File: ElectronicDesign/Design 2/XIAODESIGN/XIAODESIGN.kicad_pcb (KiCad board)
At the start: 2 copper layers, 92 x 50 mm, 24 parts, among them U1 XIAO-ESP32-C3-SMD, U2 MPR121QR2, U3 MPU-6050_C24112, U6 S2B-PH-K-S

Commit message: Continued Routing on the PCB Design , implementation of delay effect started and vector method for effects implemented
Vector method for effects will allow for the user to change the order of the effects using hopefully a draggable component from a previous project
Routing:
- net Net-(U2-ELE1): track 0.00 -> 50.1 mm, vias 0 -> 3
- net /INT_GYRO: track 7.58 -> 20.4 mm, vias 0 -> 2
- net Net-(U2-VREG): track 0.00 -> 8.58 mm

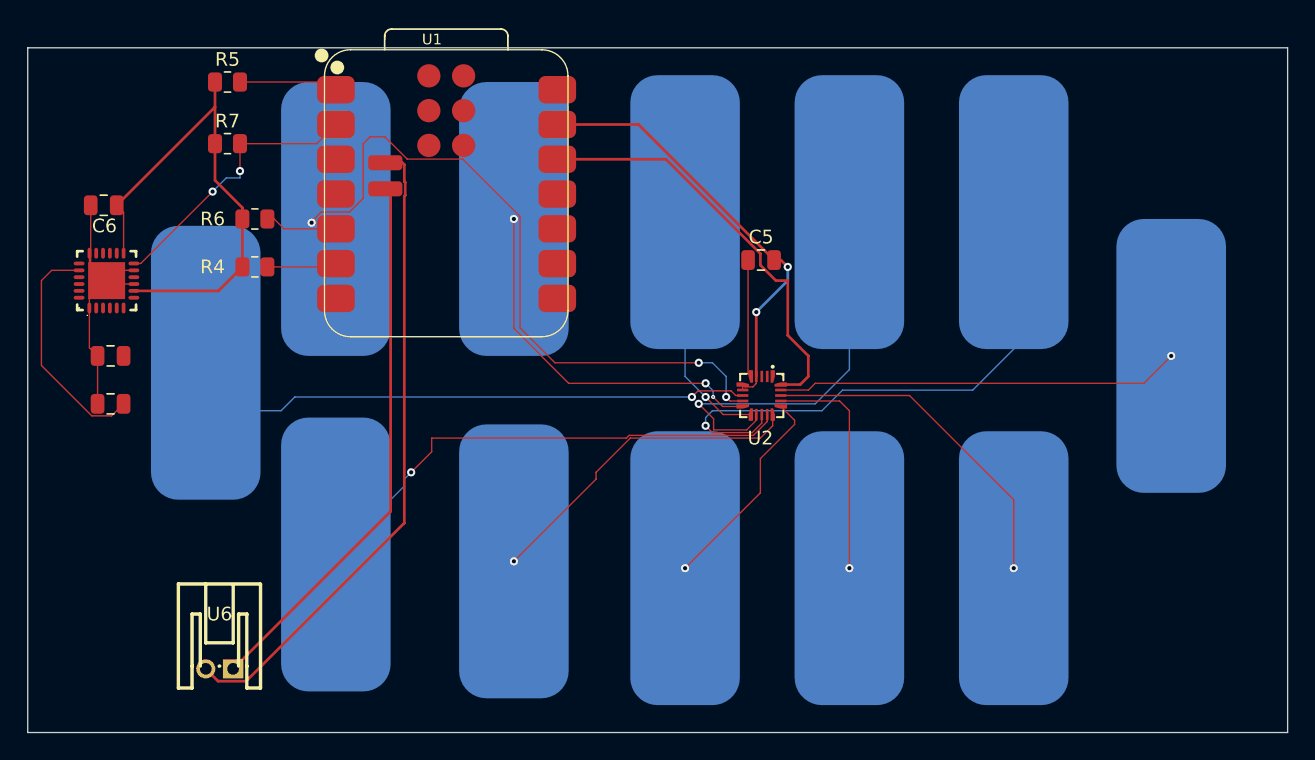
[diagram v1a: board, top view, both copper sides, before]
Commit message: Updates to draggable component , Re tracing the pcb routing to change the position of the microcontroller
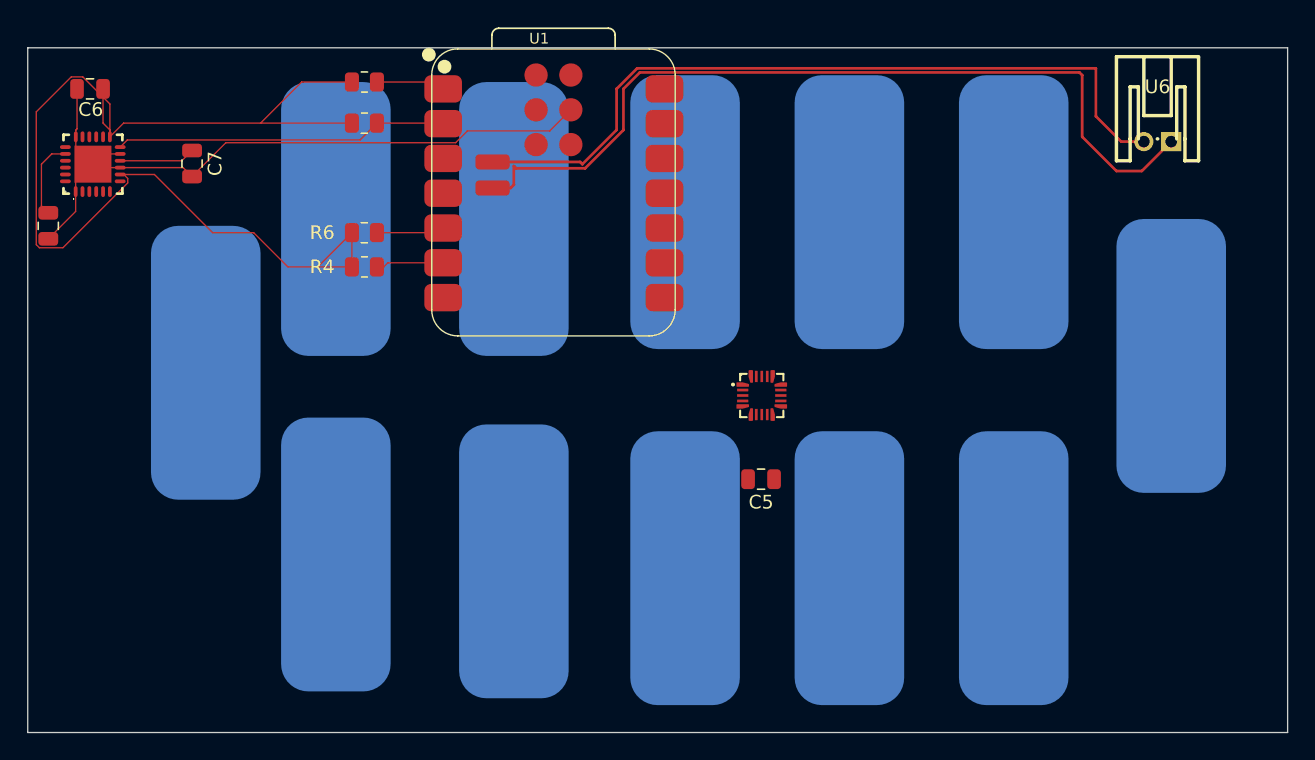
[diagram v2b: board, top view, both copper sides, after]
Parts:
- moved U6 78.6 mm to (128.5, 120.8)
- moved C5 16.0 mm to (99.5, 145.5), turned to 180 degrees
- moved C7 15.3 mm to (58.0, 122.5), turned to -90 degrees
- moved C8 13.8 mm to (47.5, 127.0), turned to 90 degrees
- moved R7 10.1 mm to (70.6, 119.5)
- moved R5 10.0 mm to (70.6, 116.5)
- moved C6 8.56 mm to (50.5, 117.0)
- moved U3 8.56 mm to (50.8, 122.5)
- moved R6 8.06 mm to (70.6, 127.5)
- moved R4 8.00 mm to (70.6, 130.0)
- moved U1 7.83 mm to (75.5, 135.1)
- turned U2 to -90 degrees
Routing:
- net Net-(U2-ELE1): track 50.1 -> 0.00 mm, vias 3 -> 0
- net Net-(U2-ELE0): track 41.4 -> 0.00 mm, vias 1 -> 0
- net Net-(U2-ELE5): track 40.4 -> 0.00 mm, vias 1 -> 0
- net Net-(U2-ELE6): track 36.9 -> 0.00 mm, vias 1 -> 0
- net Net-(U2-ELE4): track 29.7 -> 0.00 mm, vias 1 -> 0
- net Net-(U2-ELE11): track 29.5 -> 0.00 mm, vias 1 -> 0
- net Net-(U2-ELE2): track 27.3 -> 0.00 mm, vias 3 -> 0
- net Net-(U2-ELE10): track 25.2 -> 0.00 mm, vias 1 -> 0
- net Net-(U2-ELE7): track 24.1 -> 0.00 mm, vias 1 -> 0
- net +BATT: track 40.0 -> 62.3 mm
- net Net-(U2-ELE3): track 18.0 -> 0.00 mm, vias 1 -> 0
- net +3V3: track 67.7 -> 84.5 mm
- net Net-(U2-ELE9): track 16.8 -> 0.00 mm, vias 1 -> 0
- net Net-(U2-ELE8): track 15.5 -> 0.00 mm, vias 1 -> 0
- net Net-(U3-CPOUT): track 17.1 -> 5.82 mm
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
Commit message: Update to the routing
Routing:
- net GND: track 52.4 -> 157.2 mm, vias 0 -> 4
- net /SCL: track 4.96 -> 80.5 mm, vias 0 -> 2
- net Net-(U2-ELE2): track 0.00 -> 61.6 mm, vias 0 -> 1
- net /SDA: track 4.98 -> 63.9 mm, vias 0 -> 2
- net Net-(U2-ELE7): track 0.00 -> 53.9 mm, vias 0 -> 1
- net /IRQ_TS: track 5.04 -> 55.9 mm
- net Net-(U2-ELE1): track 0.00 -> 50.6 mm, vias 0 -> 1
- net Net-(U2-ELE0): track 0.00 -> 44.7 mm, vias 0 -> 1
- net Net-(U2-ELE6): track 0.00 -> 38.7 mm, vias 0 -> 1
- net Net-(U2-ELE4): track 0.00 -> 36.2 mm, vias 0 -> 1
- net Net-(U2-ELE11): track 0.00 -> 31.6 mm, vias 0 -> 1
- net Net-(U2-ELE3): track 0.00 -> 29.3 mm, vias 0 -> 1
- net Net-(U2-ELE10): track 0.00 -> 26.6 mm, vias 0 -> 1
- net +3V3: track 84.5 -> 60.4 mm, vias 0 -> 2
- net Net-(U2-ELE9): track 0.00 -> 23.6 mm, vias 0 -> 1
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
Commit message: Updated the draggable component constructor and implemented an array of the draggable components
Name of the effect connected to the draggable component is now passed through in the constructor , an array of the draggable components equal in size to the number of effects in the synth
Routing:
- net +3V3: track 60.4 -> 105.1 mm, vias 2 -> 6
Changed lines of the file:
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@@
+	)
+	(segment
+		(start 69.675 116.5)
+		(end 71.575 114.6)
+		(width 0.2)
+		(layer "F.Cu")
+		(net "+3V3")
 	)
 	(segment
@@
 	)
 	(segment
+		(start 61.5 124.5)
+		(end 62.5 123.5)
+		(width 0.2)
+		(layer "F.Cu")
+		(net "+3V3")
+	)
+	(segment
 		(start 53.01 123.25)
 		(end 54.26 124.5)
@@
 	)
 	(segment
+		(start 64.5 127.5)
+		(end 63 126)
+		(width 0.2)
+		(layer "F.Cu")
+		(net "+3V3")
+	)
+	(segment
 		(start 54.26 124.5)
 		(end 61.5 124.5)
@@
 	)
 	(segment
-		(start 61.5 124.5)
+		(start 71.575 114.6)
+		(end 86.1 114.6)
+		(width 0.2)
+		(layer "F.Cu")
+		(net "+3V3")
+	)
+	(segment
+		(start 69.675 127.5)
+		(end 64.5 127.5)
+		(width 0.2)
+		(layer "F.Cu")
+		(net "+3V3")
+	)
+	(segment
+		(start 62.5 123.5)
 		(end 63 123)
+		(width 0.2)
+		(layer "F.Cu")
+		(net "+3V3")
+	)
+	(segment
+		(start 88.5 117)
+		(end 88.5 118)
 		(width 0.2)
 		(layer "F.Cu")
@@
 	)
 	(segment
+		(start 87.5 124)
+		(end 90.58 124)
+		(width 0.2)
+		(layer "F.Cu")
+		(net "+3V3")
+	)
+	(segment
+		(start 90.58 124)
+		(end 92.5 122.08)
+		(width 0.2)
+		(layer "F.Cu")
+		(net "+3V3")
+	)
+	(segment
+		(start 86.1 114.6)
+		(end 88.5 117)
+		(width 0.2)
+		(layer "F.Cu")
+		(net "+3V3")
+	)
+	(segment
 		(start 63.5 120)
 		(end 64 119.5)
@@
 	)
 	(via
+		(at 87.5 124)
+		(size 0.6)
+		(drill 0.3)
+		(layers "F.Cu" "B.Cu")
+		(net "+3V3")
+	)
+	(via
+		(at 88.5 118)
+		(size 0.6)
+		(drill 0.3)
+		(layers "F.Cu" "B.Cu")
+		(net "+3V3")
+	)
+	(via
+		(at 63 126)
+		(size 0.6)
+		(drill 0.3)
+		(layers "F.Cu" "B.Cu")
+		(net "+3V3")
+	)
+	(via
+		(at 62.5 123.5)
+		(size 0.6)
+		(drill 0.3)
+		(layers "F.Cu" "B.Cu")
+		(net "+3V3")
+	)
+	(via
 		(at 63 122)
 		(size 0.6)
@@
 		(drill 0.3)
 		(layers "F.Cu" "B.Cu")
+		(net "+3V3")
+	)
+	(segment
+		(start 63 126)
+		(end 63 124)
+		(width 0.2)
+		(layer "B.Cu")
+		(net "+3V3")
+	)
+	(segment
+		(start 87 124)
+		(end 87.5 124)
+		(width 0.2)
+		(layer "B.Cu")
 		(net "+3V3")
 	)
@@
 		(width 0.2)
 		(layer "B.Cu")
+		(net "+3V3")
+	)
+	(segment
+		(start 63 124)
+		(end 62.5 123.5)
+		(width 0.2)
+		(layer "B.Cu")
+		(net "+3V3")
+	)
+	(segment
+		(start 88.5 118)
+		(end 88.292893 118)
+		(width 0.2)
+		(layer "B.Cu")
+		(net "+3V3")
+	)
+	(segment
+		(start 87 119.292893)
+		(end 87 124)
+		(width 0.2)
+		(layer "B.Cu")
+		(net "+3V3")
+	)
+	(segment
+		(start 88.292893 118)
+		(end 87 119.292893)
+		(width 0.2)
+		(layer "B.Cu")

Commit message: Update to wiring and draggable component implementation
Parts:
- added REF**: MountingHole_3.5mm, MountingHole:MountingHole_3.5mm, F.Cu at (50.5, 134.5)
- added REF**: MountingHole_3.5mm, MountingHole:MountingHole_3.5mm, F.Cu at (131.0, 157.5)
- moved U6 2.35 mm to (128.5, 118.5), turned to 180 degrees
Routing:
- net +BATT: track 62.3 -> 57.6 mm
- net -BATT: track 56.5 -> 56.0 mm
